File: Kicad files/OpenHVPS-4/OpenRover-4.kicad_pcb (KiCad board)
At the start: 2 copper layers, 40.6 x 20.8 mm, 71 parts, among them J1 Conn_01x03_Male, Q1 FQT7N10, Q2 BC846A, Q3 MMDT3906, U1 MAX6008AEUR+T, U2 74HC14, U3 MAX4162, U4 CD14538BM

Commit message: Updated BOM fro SEEED
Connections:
- net Net-(D9-Pad2) renamed no_connect_(D9-Pad2)
- net Net-(U1-Pad3) renamed no_connect_(U1-Pad3)
- net Net-(U4-Pad10) renamed no_connect_(U4-Pad10)
- net Net-(U4-Pad14) renamed no_connect_(U4-Pad14)
- net Net-(U4-Pad7) renamed no_connect_(U4-Pad7)
- net Net-(U4-Pad9) renamed no_connect_(U4-Pad9)
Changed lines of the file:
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@@
   (net 40 "Net-(R7-Pad2)")
   (net 41 "Net-(R10-Pad2)")
-  (net 42 "Net-(D9-Pad2)")
+  (net 42 "no_connect_(D9-Pad2)")
   (net 43 "Net-(F1-Pad1)")
   (net 44 "Net-(C22-Pad1)")
-  (net 45 "Net-(U1-Pad3)")
-  (net 46 "Net-(U4-Pad7)")
-  (net 47 "Net-(U4-Pad9)")
-  (net 48 "Net-(U4-Pad10)")
-  (net 49 "Net-(U4-Pad14)")
+  (net 45 "no_connect_(U1-Pad3)")
+  (net 46 "no_connect_(U4-Pad7)")
+  (net 47 "no_connect_(U4-Pad9)")
+  (net 48 "no_connect_(U4-Pad10)")
+  (net 49 "no_connect_(U4-Pad14)")
   (footprint "Resistor_SMD:R_0805_2012Metric" (layer "F.Cu")
     (at 128.5 71.5 90)
@@
       (net 17 "Net-(C20-Pad2)") (pinfunction "K"))
     (pad "2" smd roundrect (at -0.9375 0.95 90) (locked) (size 1.475 0.6) (layers "F.Cu" "F.Paste" "F.Mask") (roundrect_rratio 0.25)
-      (net 42 "Net-(D9-Pad2)") (pinfunction "A"))
+      (net 42 "no_connect_(D9-Pad2)") (pinfunction "A"))
     (pad "3" smd roundrect (at 0.9375 0 90) (locked) (size 1.475 0.6) (layers "F.Cu" "F.Paste" "F.Mask") (roundrect_rratio 0.25)
       (net 25 "Net-(C21-Pad2)") (pinfunction "K"))
@@
       (net 31 "Net-(D2-Pad2)") (pinfunction "Q"))
     (pad "7" smd roundrect (at -2.475 -3.175 270) (locked) (size 1.95 0.6) (layers "B.Cu" "B.Paste" "B.Mask") (roundrect_rratio 0.25)
-      (net 46 "Net-(U4-Pad7)") (pinfunction "~Q"))
+      (net 46 "no_connect_(U4-Pad7)") (pinfunction "~Q"))
     (pad "8" smd roundrect (at -2.475 -4.445 270) (locked) (size 1.95 0.6) (layers "B.Cu" "B.Paste" "B.Mask") (roundrect_rratio 0.25)
       (net 3 "GND") (pinfunction "VSS"))
     (pad "9" smd roundrect (at 2.475 -4.445 270) (locked) (size 1.95 0.6) (layers "B.Cu" "B.Paste" "B.Mask") (roundrect_rratio 0.25)
-      (net 47 "Net-(U4-Pad9)") (pinfunction "~Q"))
+      (net 47 "no_connect_(U4-Pad9)") (pinfunction "~Q"))
     (pad "10" smd roundrect (at 2.475 -3.175 270) (locked) (size 1.95 0.6) (layers "B.Cu" "B.Paste" "B.Mask") (roundrect_rratio 0.25)
-      (net 48 "Net-(U4-Pad10)") (pinfunction "Q"))
+      (net 48 "no_connect_(U4-Pad10)") (pinfunction "Q"))
     (pad "11" smd roundrect (at 2.475 -1.905 270) (locked) (size 1.95 0.6) (layers "B.Cu" "B.Paste" "B.Mask") (roundrect_rratio 0.25)
       (net 3 "GND") (pinfunction "Clk-"))
@@
       (net 3 "GND") (pinfunction "R"))
     (pad "14" smd roundrect (at 2.475 1.905 270) (locked) (size 1.95 0.6) (layers "B.Cu" "B.Paste" "B.Mask") (roundrect_rratio 0.25)
-      (net 49 "Net-(U4-Pad14)") (pinfunction "RxCx"))
+      (net 49 "no_connect_(U4-Pad14)") (pinfunction "RxCx"))
     (pad "15" smd roundrect (at 2.475 3.175 270) (locked) (size 1.95 0.6) (layers "B.Cu" "B.Paste" "B.Mask") (roundrect_rratio 0.25)
       (net 3 "GND") (pinfunction "VSS"))
@@
       (net 3 "GND") (pinfunction "OUT"))
     (pad "3" smd roundrect (at 0.9375 0 180) (locked) (size 1.475 0.6) (layers "B.Cu" "B.Paste" "B.Mask") (roundrect_rratio 0.25)
-      (net 45 "Net-(U1-Pad3)") (pinfunction "GND"))
+      (net 45 "no_connect_(U1-Pad3)") (pinfunction "GND"))
     (model "${KICAD6_3DMODEL_DIR}/Package_TO_SOT_SMD.3dshapes/SOT-23.wrl"
       (offset (xyz 0 0 0))

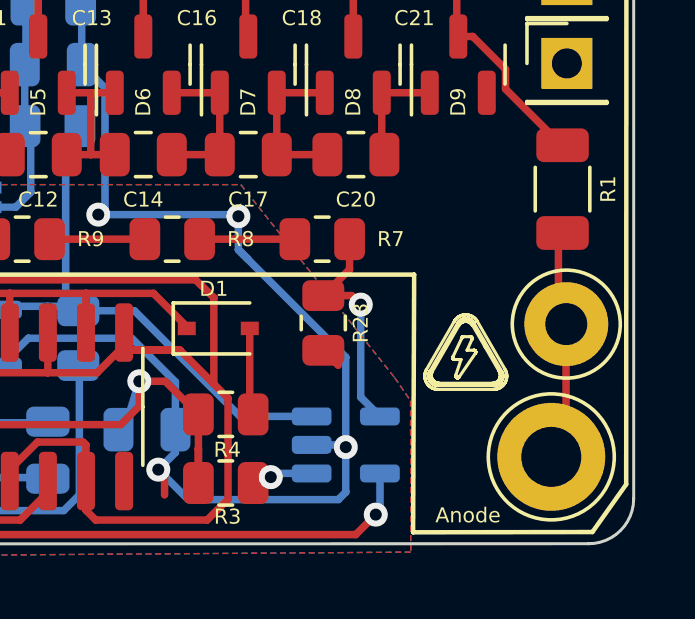
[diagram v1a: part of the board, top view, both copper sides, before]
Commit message: Added logos
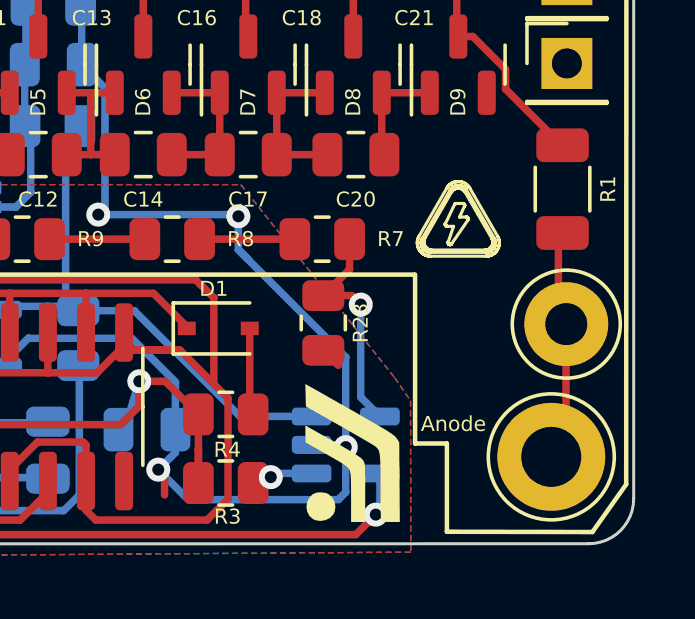
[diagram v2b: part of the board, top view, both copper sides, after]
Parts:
- added G***: LOGO, Symbol:Safecast logo very small, F.Cu at (157.5, 75.0)
- added G***: LOGO, Symbol:Safecast logo very small, B.Cu at (149.5, 67.0)
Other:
- board text added: "SAFECAST"
- board text removed: "Safecast"

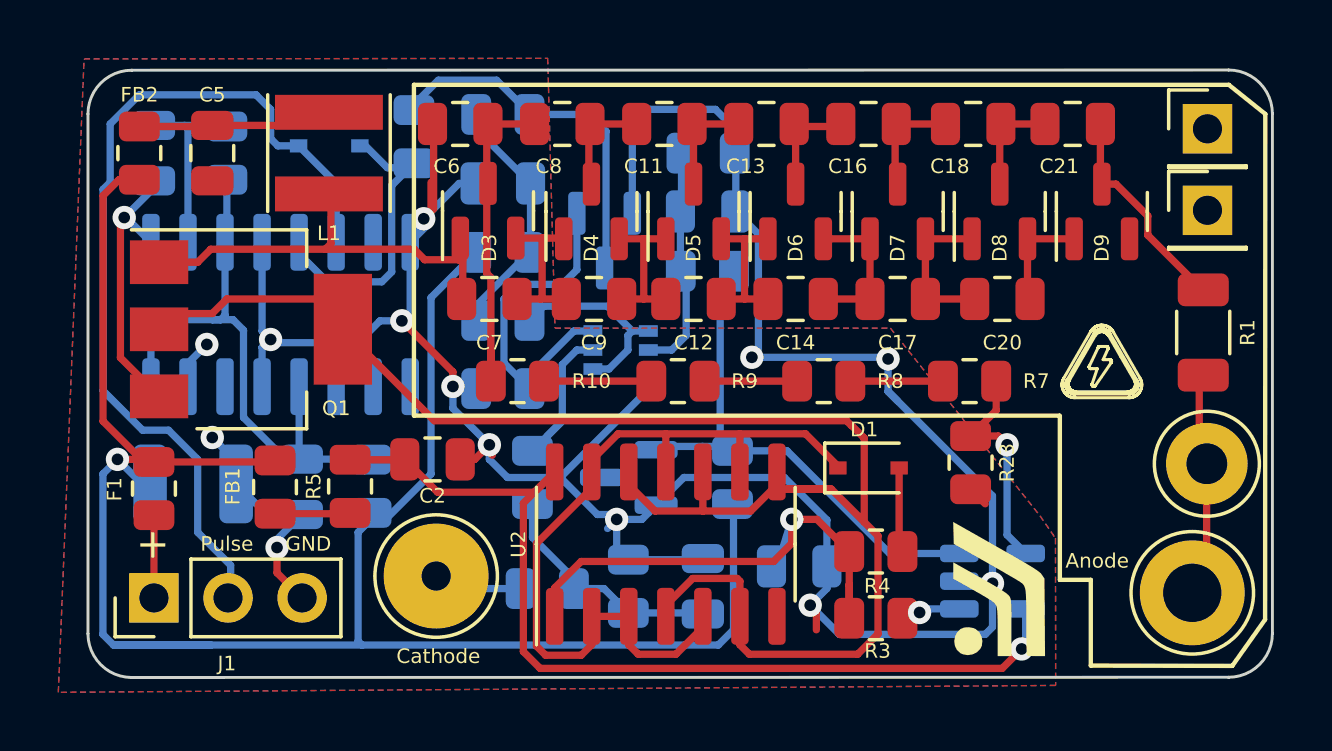
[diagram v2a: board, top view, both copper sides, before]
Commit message: Update the connectors sizes and two pin header
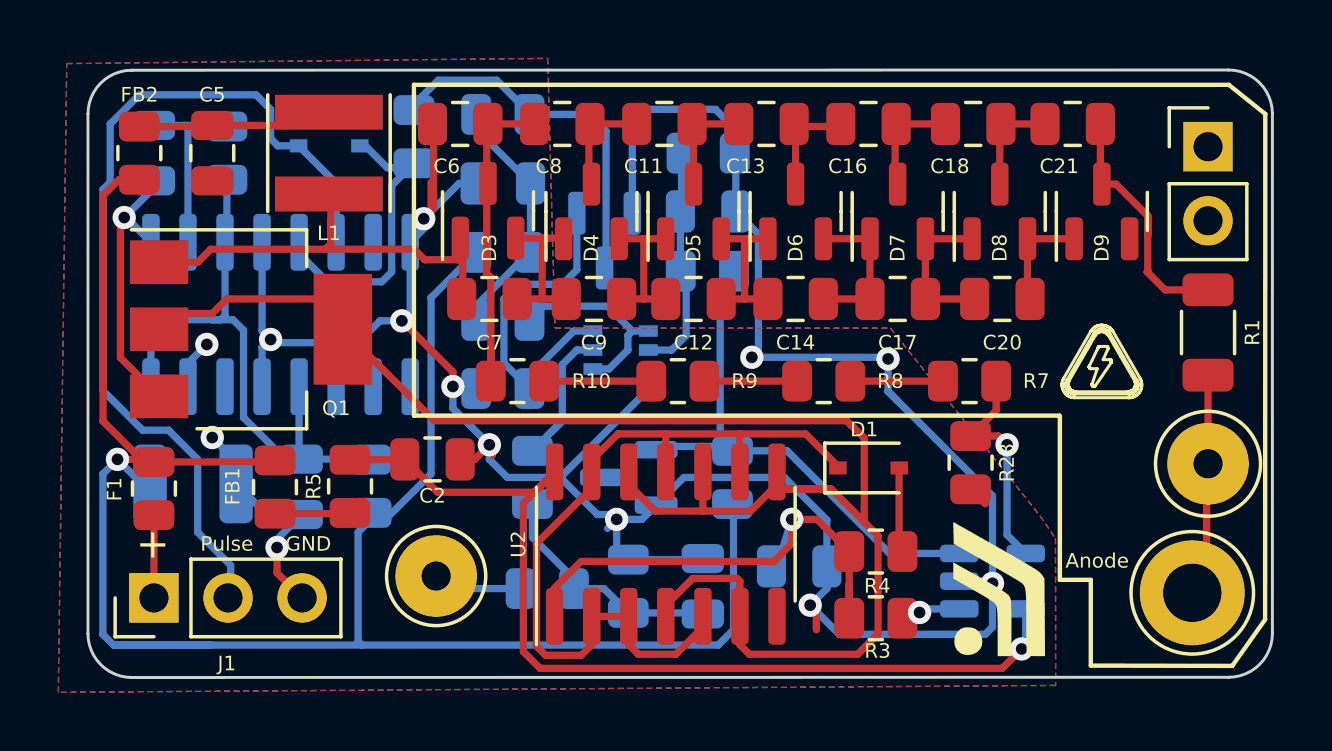
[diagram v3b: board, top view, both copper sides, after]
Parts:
- removed the REF** at (164.6, 59.2)
- removed the REF** at (164.6, 62.0)
- added REF**: PinHeader_1x02_P2.54mm_Vertical, Connector_PinHeader_2.54mm:PinHeader_1x02_P2.54mm_Vertical, F.Cu at (164.6, 59.8)
- H1: footprint TestPoint:TestPoint_Loop_D3.80mm_Drill2.0mm -> TestPoint:TestPoint_Loop_D2.60mm_Drill1.4mm_Beaded
- moved R1 0.16 mm to (164.6, 66.2)
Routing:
- net Net-(C21-Pad2): track 7.39 -> 9.17 mm
